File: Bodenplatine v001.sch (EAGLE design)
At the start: 113 parts, among them K1 RY612012, K2 RY612012, K3 RY612012, K4 RY612012, K5 RY612012, K6 RY612012, K7 RY612012, K8 RY612012, K9 RY612012, Q1 BC846, Q2 BC846, Q3 BC846, Q4 BC846, Q5 BC846, Q6 BC846, Q7 BC846, Q8 BC846, Q9 BC846, X1 SPRINGCON_AST125_5X2, X10 SPRINGCON_AST125_3X2, X11 SPRINGCON_AST125_4X2, X12 SPRINGCON_AST125_4X2, X13 SPRINGCON_AST125_5X2, X14 236-403, X15 236-402, X2 SPRINGCON_AST125_5X2, X3 SPRINGCON_AST125_5X2, X4 SPRINGCON_AST125_5X2, X5 SPRINGCON_AST125_5X2, X6 SPRINGCON_AST125_5X2, X7 SPRINGCON_AST125_5X2, X8 SPRINGCON_AST125_5X2, X9 SPRINGCON_AST125_5X2

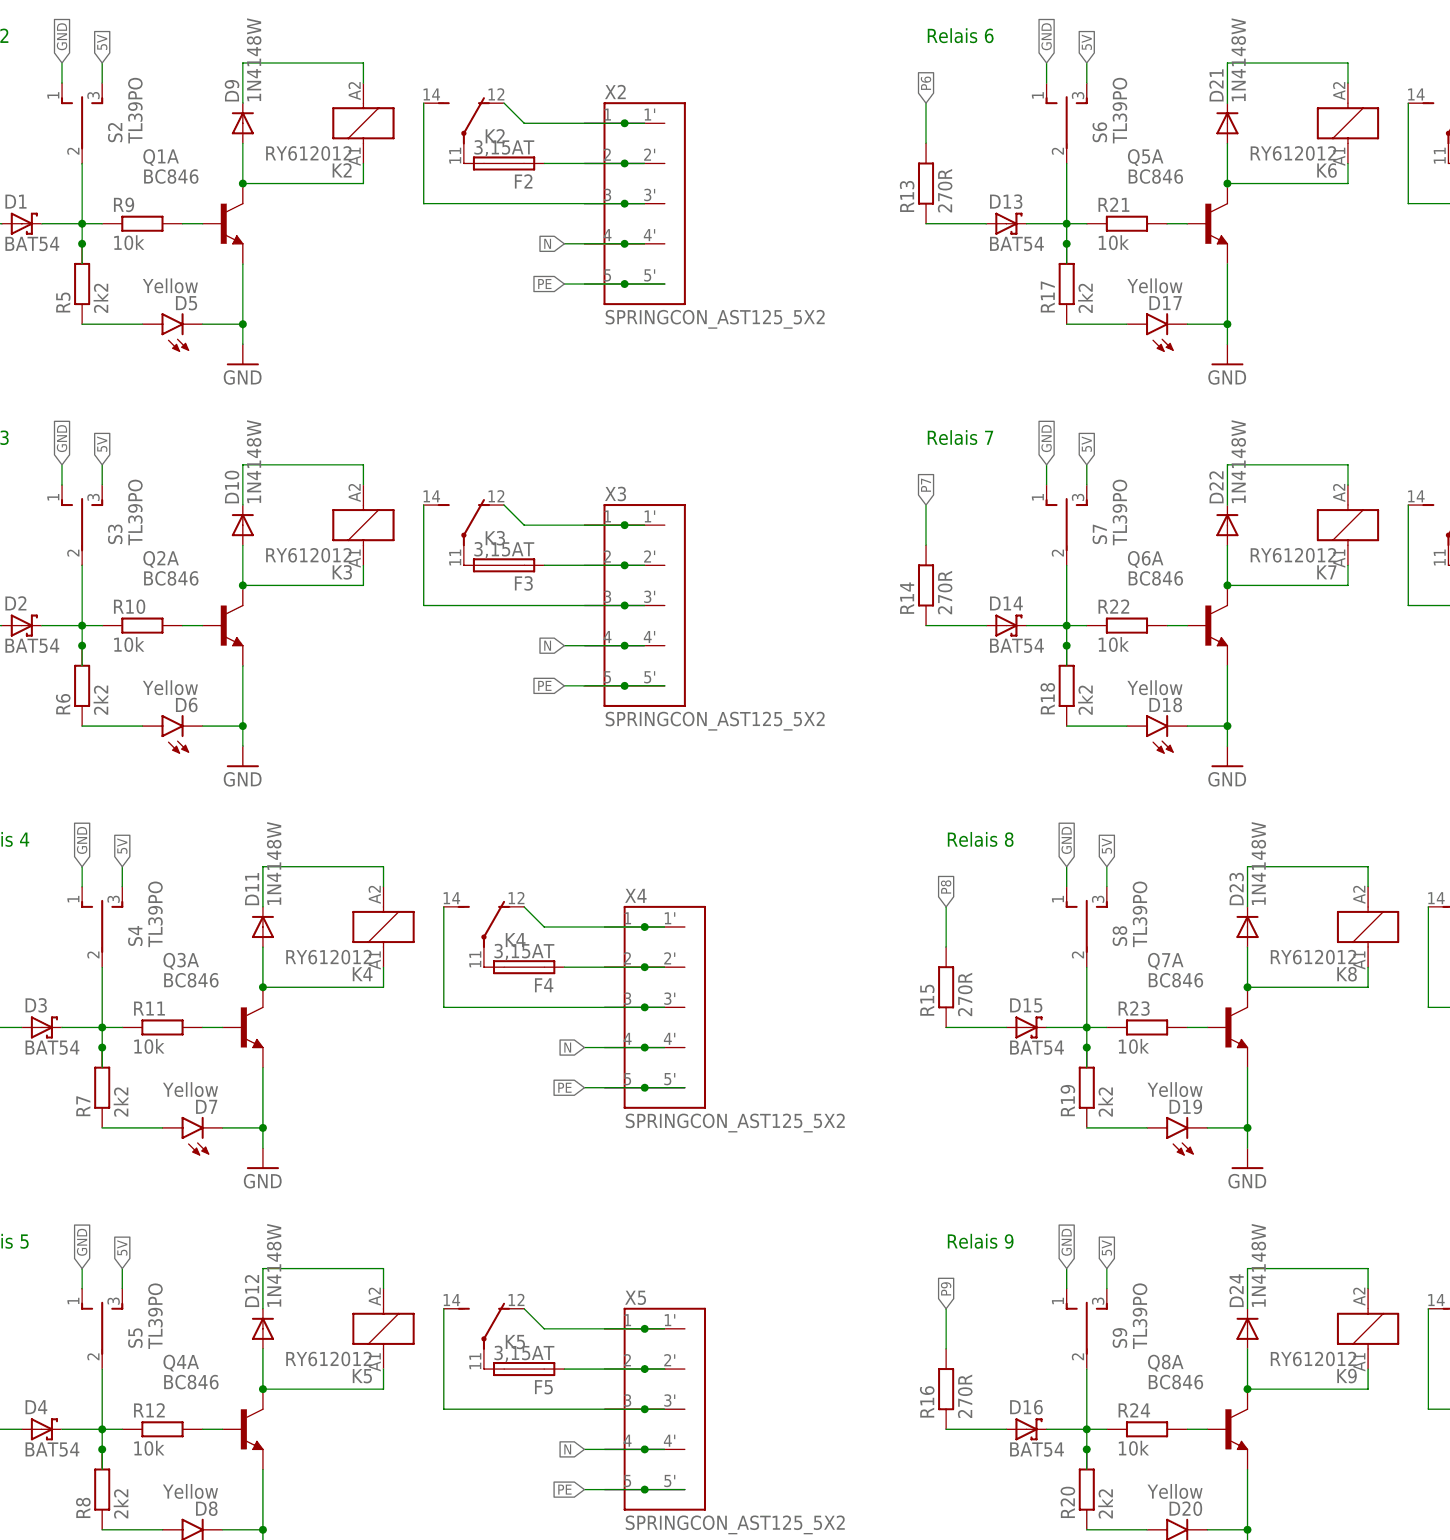
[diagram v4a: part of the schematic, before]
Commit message: BC486 ausgetauscht
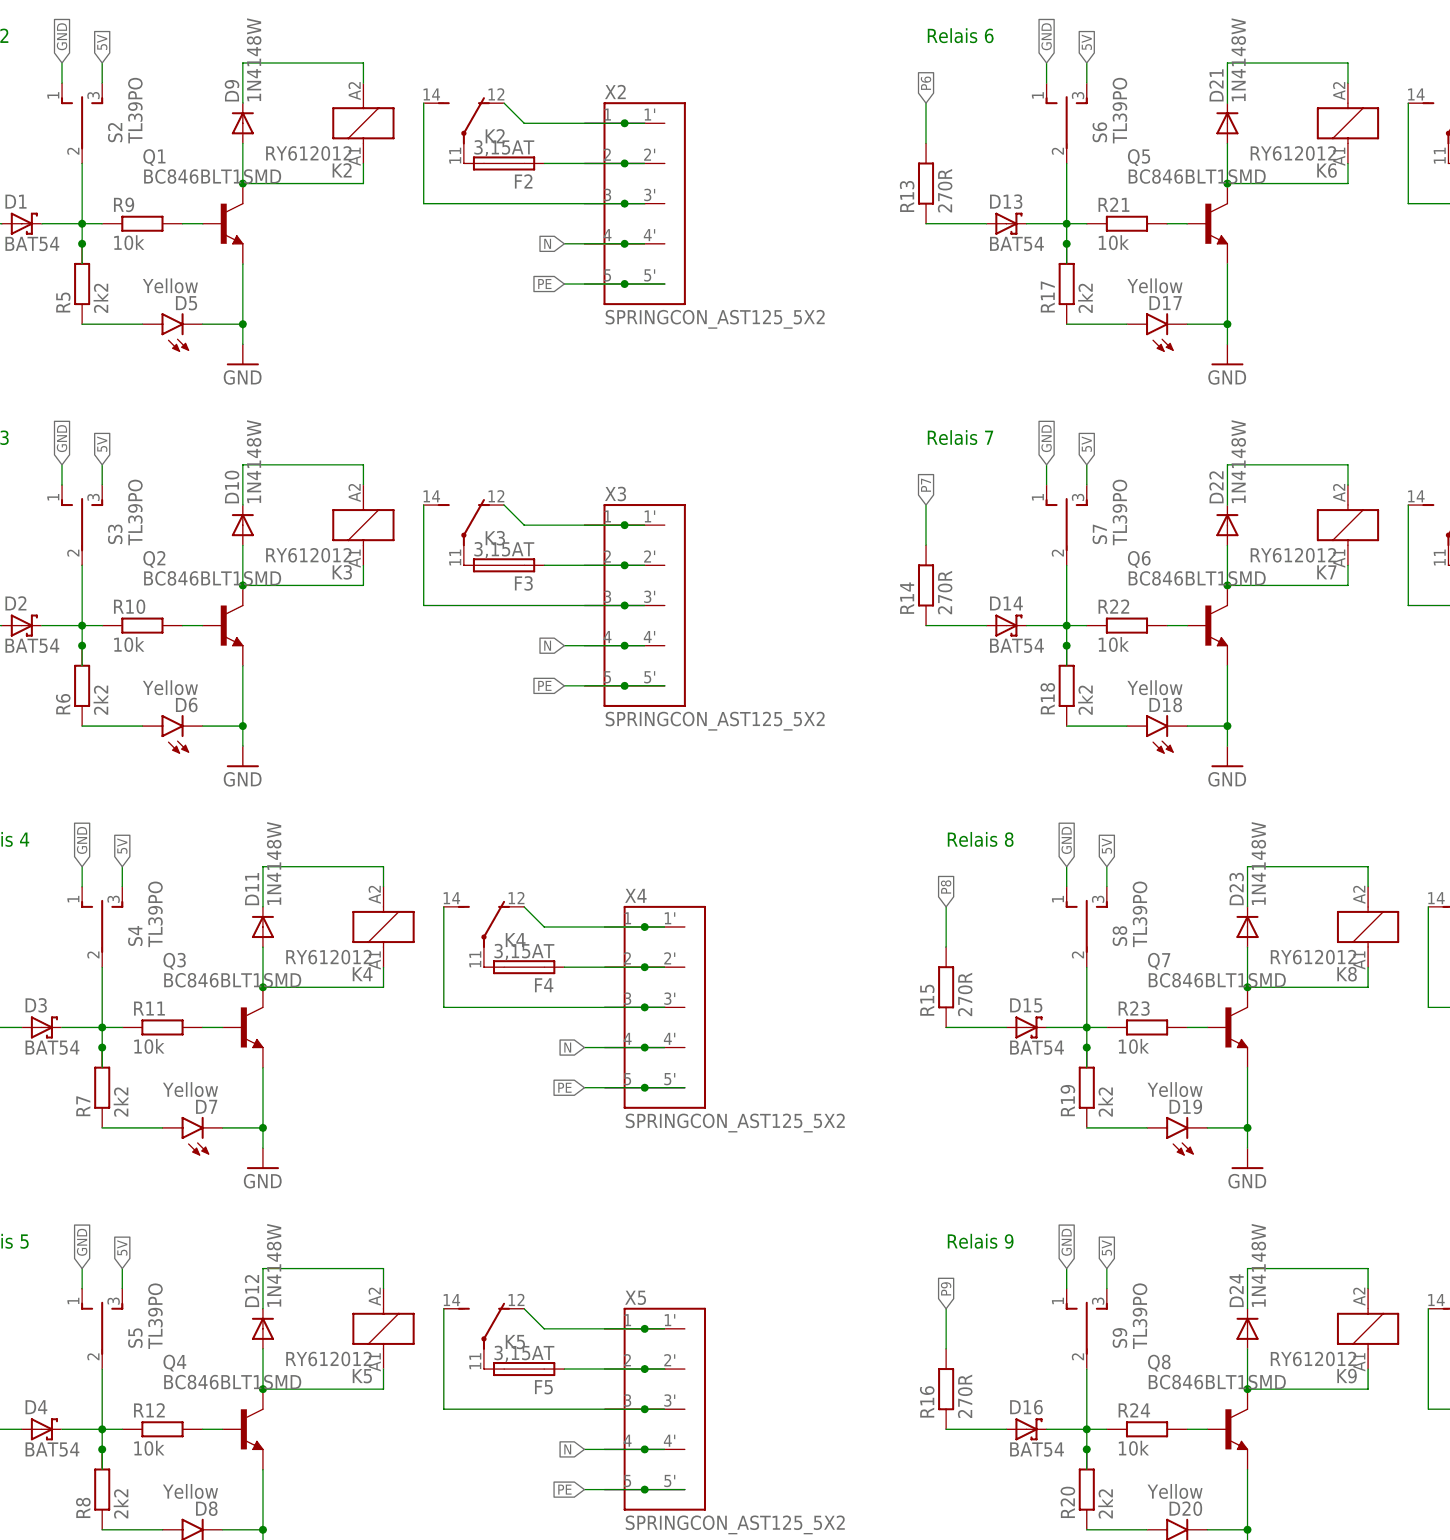
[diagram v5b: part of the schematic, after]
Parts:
- D1, D10, D11, D12, D13, D14, D15, D16, D17, D18, D19, D2, D20, D21, D22, D23, D24, D25, D26, D27, D3, D4, D5, D6, D7, D8, D9, H1, H2, H3, H4, JP1, S1, S2, S3, S4, S5, S6, S7, S8, S9, X1, X10, X11, X12, X13, X2, X3, X4, X5, X6, X7, X8, X9: OC_FARNELL (none) -> unknown
- Q1, Q2, Q3, Q4, Q5, Q6, Q7, Q8: value BC846 -> BC846BLT1SMD; device AWJLEagleLib:BC846BS" -> xMZ-Mod-Touch-Bodenplatine:BC846BLT1SMD; OC_FARNELL (none) -> 2317836
- Q9: MF (none) -> ON SEMICONDUCTOR; MPN (none) -> BC846BWT1G; OC_FARNELL (none) -> 2317836
- R1, R13, R14, R15, R16, R2, R25, R3, R4: MF (none) -> MULTICOMP; MPN (none) -> MC01W08055270R; OC_FARNELL (none) -> 9334254
- R10, R11, R12, R21, R22, R23, R24, R27, R9: MF (none) -> TE CONNECTIVITY / NEOHM; MPN (none) -> CPF0603B10KE1; OC_FARNELL (none) -> 1697388
- R17, R18, R19, R20, R26, R5, R6, R7, R8: MF (none) -> MULTICOMP; MPN (none) -> MC0063W060352K2; OC_FARNELL (none) -> 9331913
- X14: MF (none) -> WAGO; MPN (none) -> 236-403; OC_FARNELL (none) -> 1283527
- X15: MF (none) -> WAGO; MPN (none) -> 236-402; OC_FARNELL (none) -> 1283526
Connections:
- net GND: now also Q1.E, Q2.E, Q3.E, Q4.E, Q5.E, Q6.E, Q7.E, Q8.E; no longer Q1A.E, Q2A.E, Q3A.E, Q4A.E, Q5A.E, Q6A.E, Q7A.E, Q8A.E
- net N$10: now also Q1.B; no longer Q1A.B
- net N$16: now also Q2.B; no longer Q2A.B
- net N$18: now also Q2.C; no longer Q2A.C
- net N$26: now also Q3.B; no longer Q3A.B
- net N$28: now also Q3.C; no longer Q3A.C
- net N$36: now also Q4.B; no longer Q4A.B
- net N$38: now also Q4.C; no longer Q4A.C
- net N$46: now also Q5.B; no longer Q5A.B
- net N$48: now also Q5.C; no longer Q5A.C
- net N$5: now also Q1.C; no longer Q1A.C
- net N$56: now also Q6.B; no longer Q6A.B
- net N$58: now also Q6.C; no longer Q6A.C
- net N$66: now also Q7.B; no longer Q7A.B
- net N$68: now also Q7.C; no longer Q7A.C
- net N$76: now also Q8.B; no longer Q8A.B
- net N$78: now also Q8.C; no longer Q8A.C

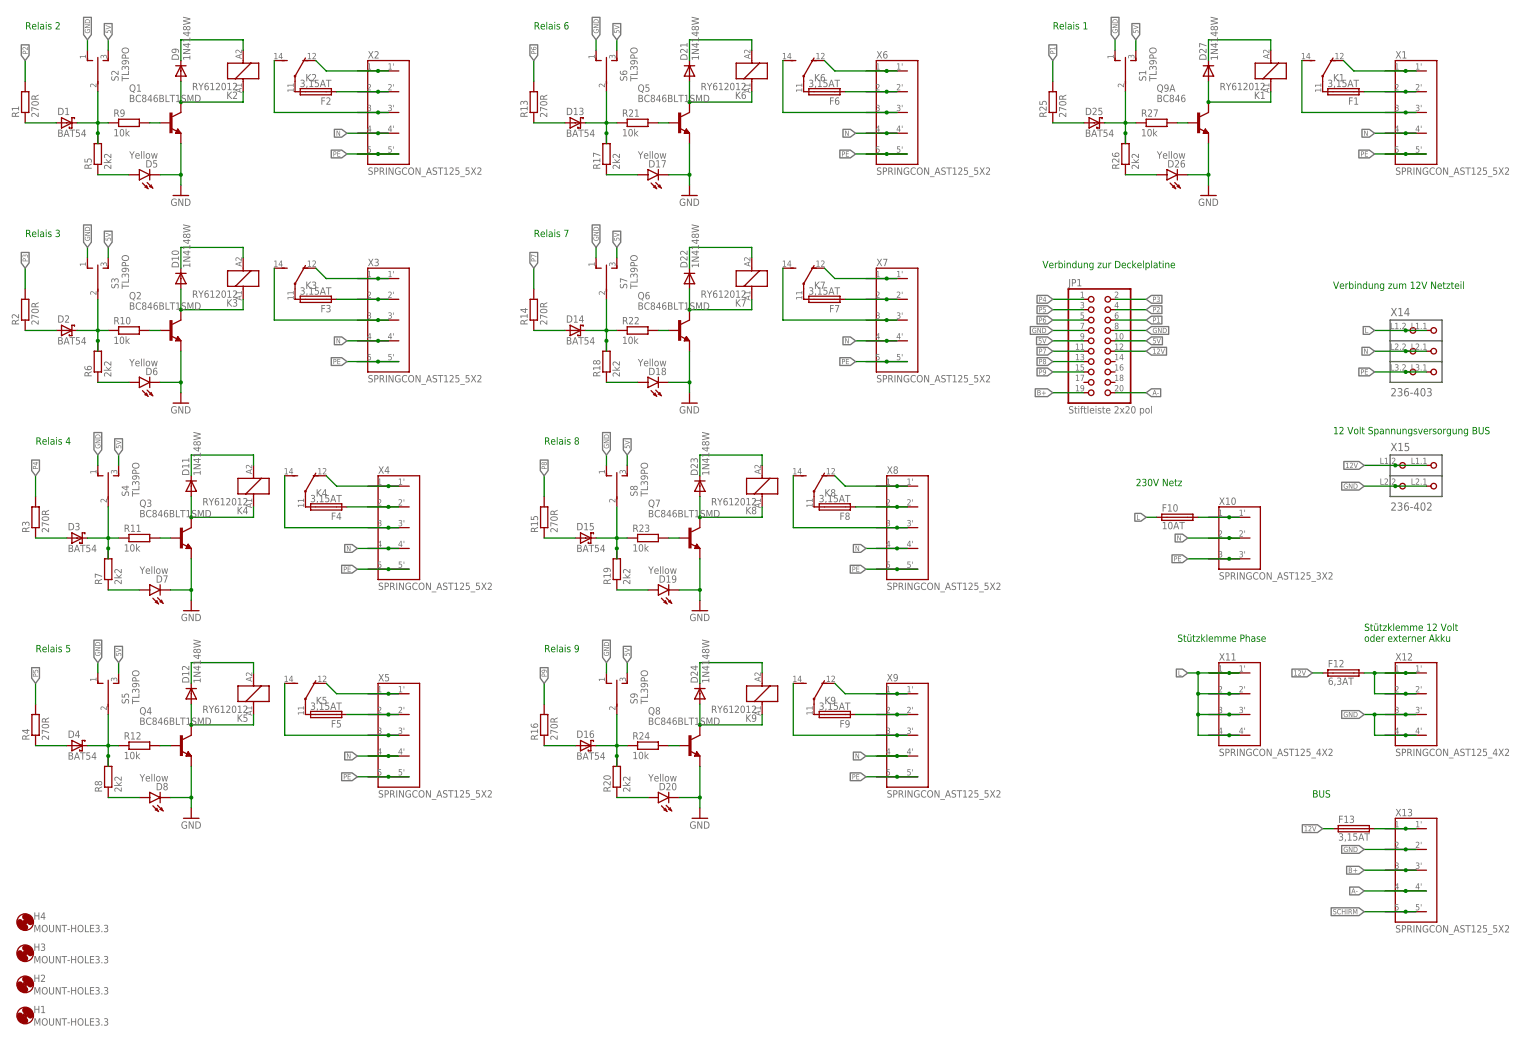
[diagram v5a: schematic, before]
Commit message: Korrektur zum letzten Commit, Ein BC486 vergessen
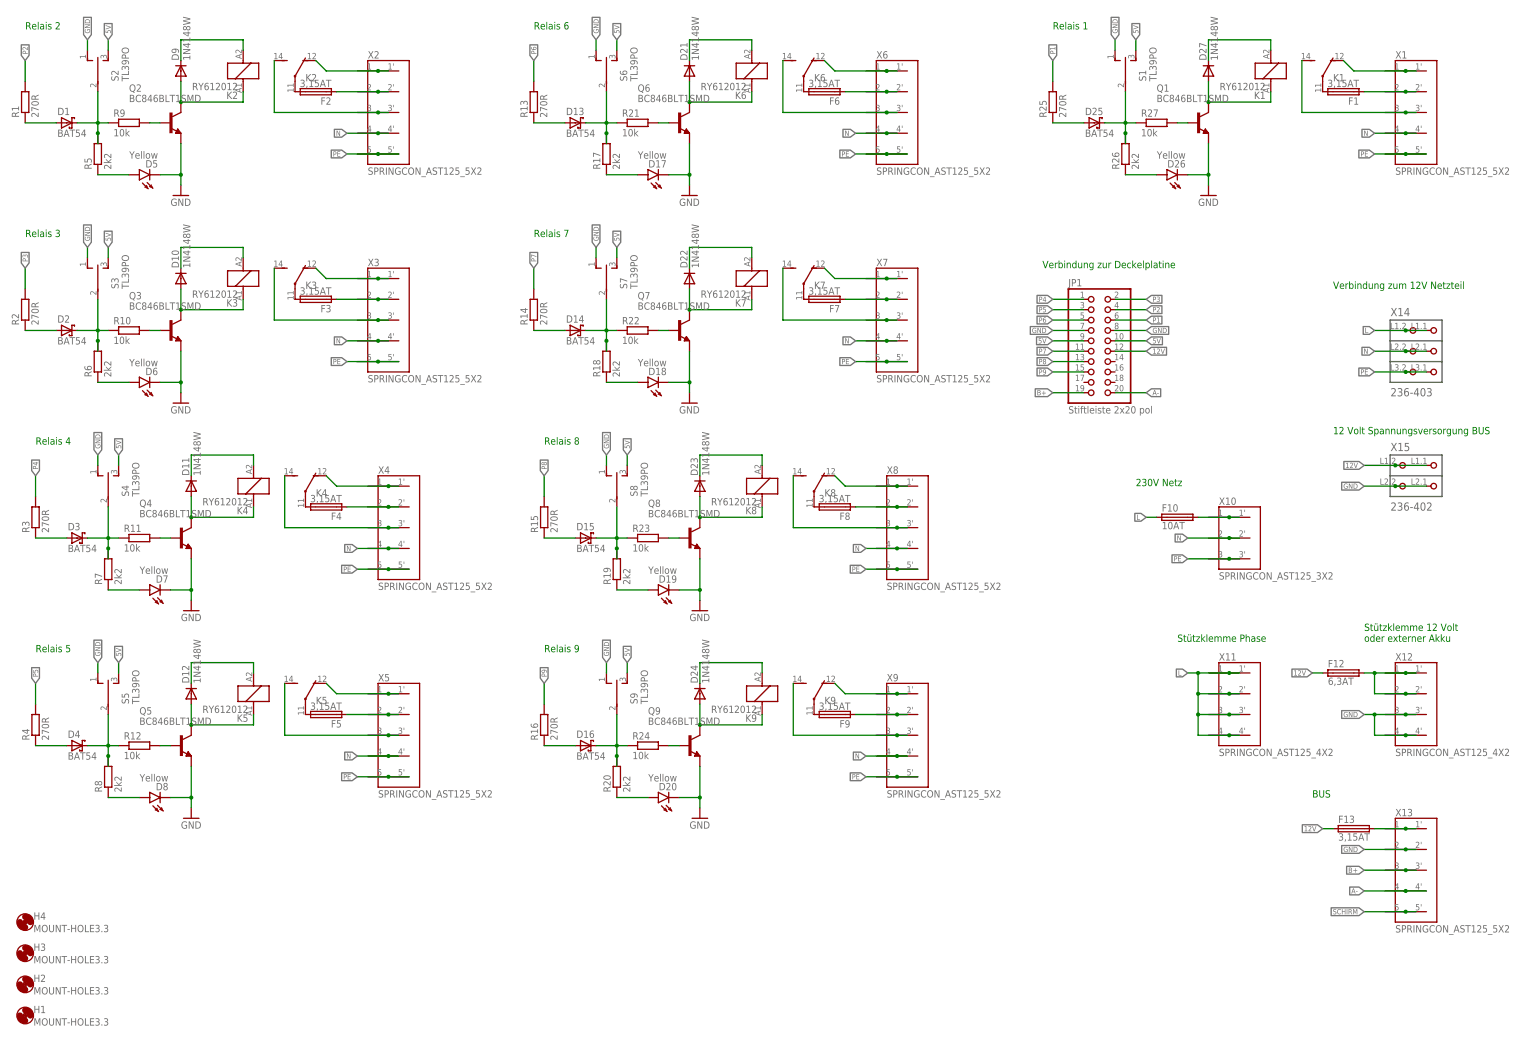
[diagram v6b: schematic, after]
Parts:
- Q9: value BC846 -> BC846BLT1SMD; device AWJLEagleLib:BC846BS" -> xMZ-Mod-Touch-Bodenplatine:BC846BLT1SMD; MF ON SEMICONDUCTOR -> (none); MPN BC846BWT1G -> (none)
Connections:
- net GND: now also Q9.E; no longer Q9A.E
- net N$10: now also Q2.B; no longer Q1.B
- net N$16: now also Q3.B; no longer Q2.B
- net N$18: now also Q3.C; no longer Q2.C
- net N$26: now also Q4.B; no longer Q3.B
- net N$28: now also Q4.C; no longer Q3.C
- net N$36: now also Q5.B; no longer Q4.B
- net N$38: now also Q5.C; no longer Q4.C
- net N$46: now also Q6.B; no longer Q5.B
- net N$48: now also Q6.C; no longer Q5.C
- net N$5: now also Q2.C; no longer Q1.C
- net N$56: now also Q7.B; no longer Q6.B
- net N$58: now also Q7.C; no longer Q6.C
- net N$66: now also Q8.B; no longer Q7.B
- net N$68: now also Q8.C; no longer Q7.C
- net N$76: now also Q9.B; no longer Q8.B
- net N$78: now also Q9.C; no longer Q8.C
- net N$86: now also Q1.B; no longer Q9A.B
- net N$88: now also Q1.C; no longer Q9A.C
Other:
- moved on the sheet: Q1, Q2, Q3, Q4, Q5, Q6, Q7, Q8
